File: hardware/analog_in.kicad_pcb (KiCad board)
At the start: 2 copper layers, 30 x 35 mm, 37 parts, among them P1 CON-SENSOR2, P2 CONN_5, P3 BOOT, P4 DEBUG, U1 XMC1XXX24, U2 TLV272IS, U3 DRILL, U4 DRILL, U5 DRILL, U6 DRILL

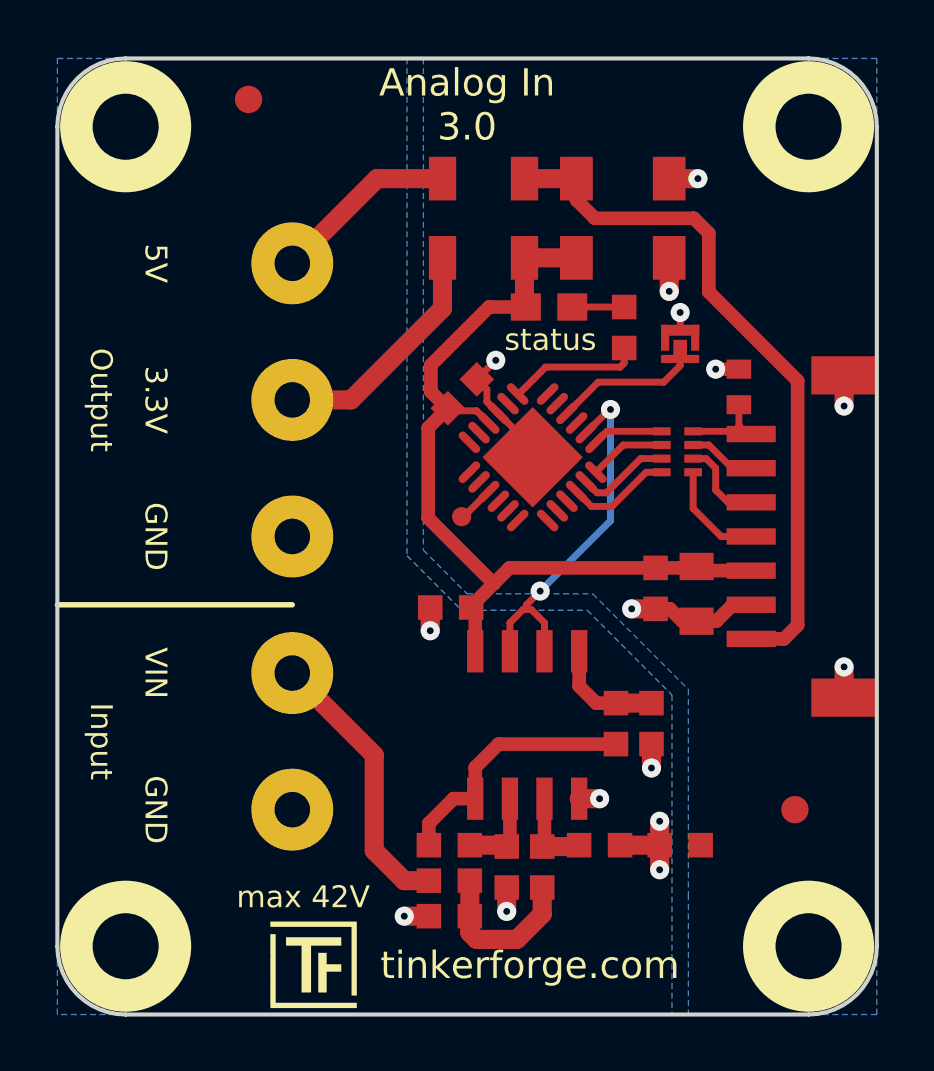
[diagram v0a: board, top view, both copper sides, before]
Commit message: small routing changes
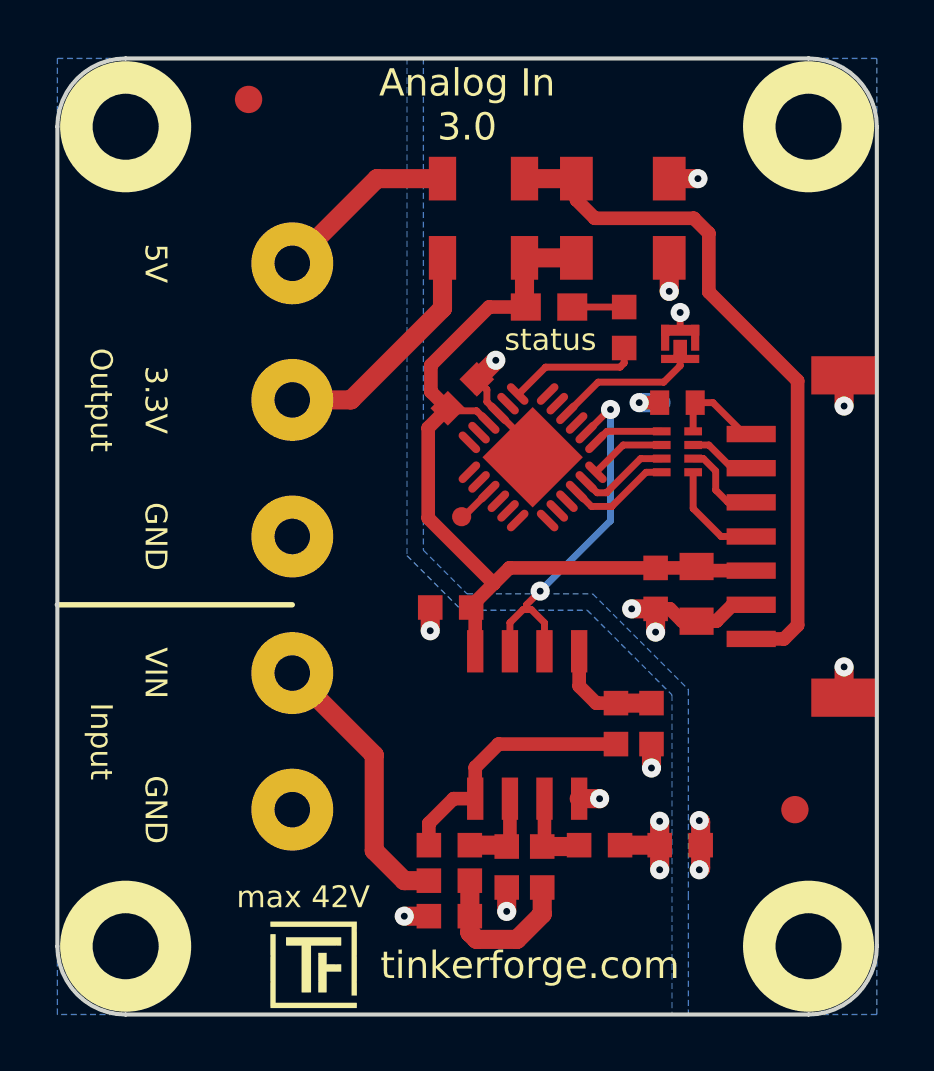
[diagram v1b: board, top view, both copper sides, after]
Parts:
- moved C5 2.32 mm to (198.2, 107.2), turned to 180 degrees
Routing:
- net GND: track 22.6 -> 26.1 mm, vias 8 -> 11
- net Net-(C5-Pad1): track 3.66 -> 4.26 mm
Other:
- board text added: "Copyright Tinkerforge GmbH 2017. This documentation describes Open Hardware and is licensed under the CERN OHL v. 1.1. You may redistribute and modify this documentation under the terms of the CERN OHL v.1.1. (http://ohwr.org/cernohl). This documentation is distributed WITHOUT ANY EXPRESS OR IMPLIED WARRANTY, INCLUDING OF MERCHANTABILITY, SATISFACTORY QUALITY AND FITNESS FOR A PARTICULAR PURPOSE.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"
- board text removed: "Copyright Tinkerforge GmbH 2015. This documentation describes Open Hardware and is licensed under the CERN OHL v. 1.1. You may redistribute and modify this documentation under the terms of the CERN OHL v.1.1. (http://ohwr.org/cernohl). This documentation is distributed WITHOUT ANY EXPRESS OR IMPLIED WARRANTY, INCLUDING OF MERCHANTABILITY, SATISFACTORY QUALITY AND FITNESS FOR A PARTICULAR PURPOSE.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"
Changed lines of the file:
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@@
-(kicad_pcb (version 4) (host pcbnew 4.0.2+dfsg1-stable)
+(kicad_pcb (version 4) (host pcbnew 4.0.7-e2-6376~58~ubuntu17.04.1)
   (general
     (links 65)
-    (no_connects 2)
-    (area 175.424999 94.524999 205.575001 129.675001)
+    (no_connects 0)
+    (area 174.644999 93.744999 282.39286 160.39)
     (thickness 1.6)
     (drawings 21)
-    (tracks 182)
+    (tracks 197)
     (zones 0)
     (modules 37)
@@
   )
   (module kicad-libraries:C0402E (layer F.Cu)
-    (at 200.45 106.625 90)
+    (at 198.2 107.2 180)
     (attr smd)
-    (fp_text reference C5 (at 0 0.125 90) (layer F.Fab)
+    (fp_text reference C5 (at 0 0.125 180) (layer F.Fab)
       (effects (font (size 0.2 0.2) (thickness 0.05)))
     )
-    (fp_text value 220pF (at 0 -0.275 90) (layer F.Fab)
+    (fp_text value 220pF (at 0 -0.275 180) (layer F.Fab)
       (effects (font (size 0.2 0.2) (thickness 0.05)))
     )
@@
     (fp_line (start 0.8509 0.44958) (end -0.8509 0.44958) (layer F.Fab) (width 0.001))
     (fp_line (start -0.8509 0.44958) (end -0.8509 -0.44958) (layer F.Fab) (width 0.001))
-    (pad 1 smd rect (at -0.65 0 90) (size 0.7 0.9) (layers F.Cu F.Paste F.Mask)
+    (pad 1 smd rect (at -0.65 0 180) (size 0.7 0.9) (layers F.Cu F.Paste F.Mask)
       (net 16 "Net-(C5-Pad1)"))
-    (pad 2 smd rect (at 0.65 0 90) (size 0.7 0.9) (layers F.Cu F.Paste F.Mask)
+    (pad 2 smd rect (at 0.65 0 180) (size 0.7 0.9) (layers F.Cu F.Paste F.Mask)
       (net 2 GND))
     (model Capacitors_SMD/C_0402.wrl
@@
   (gr_line (start 184.1 114.6) (end 175.5 114.6) (angle 90) (layer F.SilkS) (width 0.2))
   (gr_line (start 175.5 127.1) (end 175.5 97.1) (angle 90) (layer Edge.Cuts) (width 0.15))
-  (gr_text "Copyright Tinkerforge GmbH 2015.\nThis documentation describes Open Hardware and is licensed under the\nCERN OHL v. 1.1.\nYou may redistribute and modify this documentation under the terms of the\nCERN OHL v.1.1. (http://ohwr.org/cernohl). This documentation is distributed\nWITHOUT ANY EXPRESS OR IMPLIED WARRANTY, INCLUDING OF\nMERCHANTABILITY, SATISFACTORY QUALITY AND FITNESS FOR A\nPARTICULAR PURPOSE. Please see the CERN OHL v.1.1 for applicable\nconditions" (at 258.45 154.05) (layer Cmts.User)
+  (gr_text "Copyright Tinkerforge GmbH 2017.\nThis documentation describes Open Hardware and is licensed under the\nCERN OHL v. 1.1.\nYou may redistribute and modify this documentation under the terms of the\nCERN OHL v.1.1. (http://ohwr.org/cernohl). This documentation is distributed\nWITHOUT ANY EXPRESS OR IMPLIED WARRANTY, INCLUDING OF\nMERCHANTABILITY, SATISFACTORY QUALITY AND FITNESS FOR A\nPARTICULAR PURPOSE. Please see the CERN OHL v.1.1 for applicable\nconditions" (at 258.45 154.05) (layer Cmts.User)
     (effects (font (size 0.8 0.8) (thickness 0.2)))
   )
@@
   (segment (start 190.79754 116.30252) (end 190.79754 114.84754) (width 0.5) (layer F.Cu) (net 1))
   (segment (start 190.79754 114.84754) (end 190.65 114.7) (width 0.5) (layer F.Cu) (net 1))
-  (segment (start 190.85533 106.34467) (end 191.55 105.65) (width 0.254) (layer F.Cu) (net 2))
+  (segment (start 197.6 107.2) (end 196.8 107.2) (width 0.5) (layer F.Cu) (net 2) (status 400000))
+  (via (at 196.8 107.2) (size 0.7) (drill 0.25) (layers F.Cu B.Cu) (net 2))
+  (segment (start 196.8 107.2) (end 197.6 107.2) (width 0.7) (layer B.Cu) (net 2))
+  (segment (start 199.05 123.4) (end 199.05 124.25) (width 0.7) (layer F.Cu) (net 2))
+  (via (at 199 124.3) (size 0.7) (drill 0.25) (layers F.Cu B.Cu) (net 2))
+  (segment (start 199.05 124.25) (end 199 124.3) (width 0.7) (layer F.Cu) (net 2))
+  (segment (start 199.05 123.4) (end 199.05 122.55) (width 0.7) (layer F.Cu) (net 2))
+  (via (at 199 122.5) (size 0.7) (drill 0.25) (layers F.Cu B.Cu) (net 2))
+  (segment (start 199.05 122.55) (end 199 122.5) (width 0.7) (layer F.Cu) (net 2))
+  (segment (start 197.4 114.75) (end 197.4 115.6) (width 0.7) (layer F.Cu) (net 2))
+  (via (at 197.4 115.6) (size 0.7) (drill 0.25) (layers F.Cu B.Cu) (net 2))
+  (segment (start 190.85533 106.34467) (end 191.55 105.65) (width 0.7) (layer F.Cu) (net 2))
   (via (at 191.55 105.65) (size 0.7) (drill 0.25) (layers F.Cu B.Cu) (net 2))
   (segment (start 197.75 104.825) (end 197.75 104.575) (width 0.254) (layer F.Cu) (net 2))
@@
   (segment (start 191.644885 107.591332) (end 191.641332 107.591332) (width 0.254) (layer F.Cu) (net 2))
   (segment (start 190.85533 106.80533) (end 190.85533 106.34467) (width 0.254) (layer F.Cu) (net 2))
-  (segment (start 200.45 105.975) (end 199.6 105.975) (width 0.5) (layer F.Cu) (net 2))
-  (via (at 199.6 105.975) (size 0.7) (drill 0.25) (layers F.Cu B.Cu) (net 2))
   (segment (start 197.89926 101.9) (end 197.89926 103.12426) (width 0.7) (layer F.Cu) (net 2))
   (via (at 197.9 103.125) (size 0.7) (drill 0.25) (layers F.Cu B.Cu) (net 2))
@@
   (segment (start 199.8 112.1) (end 200.9 112.1) (width 0.254) (layer F.Cu) (net 5))
   (segment (start 198.775 111.075) (end 199.8 112.1) (width 0.254) (layer F.Cu) (net 5))
-  (segment (start 198.775 109.24892) (end 199.24892 109.24892) (width 0.254) (layer F.Cu) (net 6))
+  (segment (start 198.775 109.24892) (end 199.14892 109.24892) (width 0.254) (layer F.Cu) (net 6) (status 400000))
   (segment (start 199.6 110.4) (end 200.05 110.85) (width 0.254) (layer F.Cu) (net 6))
-  (segment (start 199.6 109.6) (end 199.6 110.4) (width 0.254) (layer F.Cu) (net 6))
-  (segment (start 199.24892 109.24892) (end 199.6 109.6) (width 0.254) (layer F.Cu) (net 6))
+  (segment (start 199.6 109.7) (end 199.6 110.4) (width 0.254) (layer F.Cu) (net 6))
+  (segment (start 199.14892 109.24892) (end 199.6 109.7) (width 0.254) (layer F.Cu) (net 6))
   (segment (start 200.05 110.85) (end 200.9 110.85) (width 0.254) (layer F.Cu) (net 6))
   (segment (start 198.775 108.75108) (end 199.35108 108.75108) (width 0.254) (layer F.Cu) (net 7))
@@
   (segment (start 194.60246 117.57746) (end 195.225 118.2) (width 0.5) (layer F.Cu) (net 15))
   (segment (start 195.95 118.2) (end 197.25 118.2) (width 0.7) (layer F.Cu) (net 15))
+  (segment (start 198.85 107.2) (end 199.5 107.2) (width 0.254) (layer F.Cu) (net 16) (status 400000))
+  (segment (start 199.5 107.2) (end 200.7 108.4) (width 0.254) (layer F.Cu) (net 16) (status 800000))
+  (segment (start 200.7 108.4) (end 201 108.4) (width 0.254) (layer F.Cu) (net 16) (status C00000))
+  (segment (start 201 108.4) (end 200.9 108.35) (width 0.254) (layer F.Cu) (net 16) (status C00000))
+  (segment (start 198.775 108.2507) (end 198.775 107.325) (width 0.254) (layer F.Cu) (net 16) (status C00000))
+  (segment (start 198.775 107.325) (end 198.8 107.3) (width 0.254) (layer F.Cu) (net 16) (status C00000))
+  (segment (start 198.8 107.3) (end 198.85 107.2) (width 0.254) (layer F.Cu) (net 16) (status C00000))
   (segment (start 200.9 108.35) (end 200.75 108.35) (width 0.254) (layer F.Cu) (net 16))
-  (segment (start 200.75 108.35) (end 200.45 108.05) (width 0.254) (layer F.Cu) (net 16))
-  (segment (start 200.45 108.05) (end 200.45 107.275) (width 0.254) (layer F.Cu) (net 16))
-  (segment (start 198.775 108.2507) (end 200.8007 108.2507) (width 0.254) (layer F.Cu) (net 16))
   (segment (start 200.8007 108.2507) (end 200.9 108.35) (width 0.254) (layer F.Cu) (net 16))
   (segment (start 200.8007 108.2507) (end 200.9 108.35) (width 0.254) (layer F.Cu) (net 16))
   (segment (start 196.25 103.7) (end 194.3501 103.7) (width 0.254) (layer F.Cu) (net 17))
+  (segment (start 198.3 105.6) (end 198.3 105.3) (width 0.254) (layer F.Cu) (net 18))
+  (segment (start 198.3 105.3) (end 198.3 105.2) (width 0.254) (layer F.Cu) (net 18))
   (segment (start 198.3 105.2) (end 198.3 105.85) (width 0.254) (layer F.Cu) (net 18))
   (segment (start 195.296447 106.45) (end 194.155115 107.591332) (width 0.254) (layer F.Cu) (net 18))
@@
       (pts
         (xy 198.6 125.2) (xy 198.6 129.6) (xy 205.5 129.6) (xy 205.5 94.6) (xy 188.9 94.6)
-        (xy 188.9 112.6) (xy 190.5 114.2) (xy 195.1 114.2) (xy 198.6 117.7) (xy 198.6 125.2)
+        (xy 188.9 112.6) (xy 190.5 114.2) (xy 195.1 114.2) (xy 198.6 117.7)
       )
     )
@@
       (pts
         (xy 188.3 112.8) (xy 190.3 114.8) (xy 194.9 114.8) (xy 198 117.9) (xy 198 129.6)
-        (xy 175.5 129.6) (xy 175.5 94.6) (xy 188.3 94.6) (xy 188.3 112.8)
+        (xy 175.5 129.6) (xy 175.5 94.6) (xy 188.3 94.6)
       )
     )
